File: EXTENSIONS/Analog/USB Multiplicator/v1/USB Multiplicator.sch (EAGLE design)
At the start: 9 parts, among them X1 USB-A

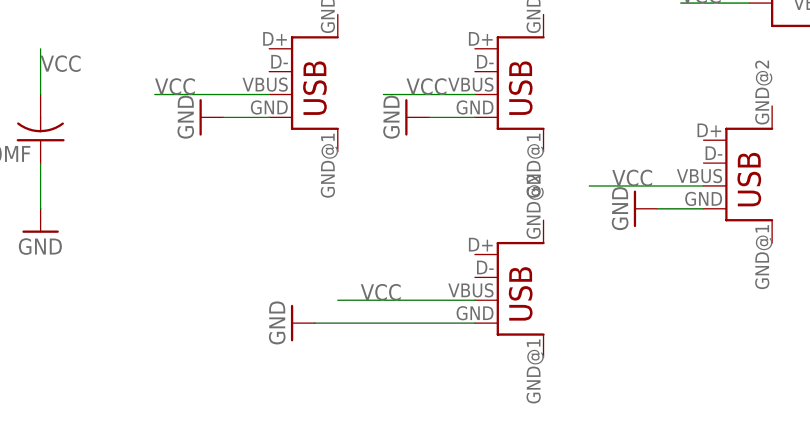
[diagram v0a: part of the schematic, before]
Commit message: Created 4017-7Segment v2
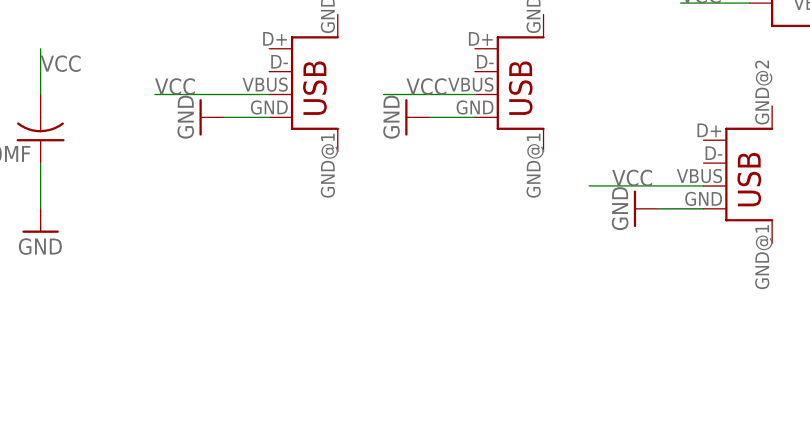
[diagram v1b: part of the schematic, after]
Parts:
- removed USB_OUT_5: USB, STUNTAZ:USB
- renumbered USB_OUT_WITH_DATA_1 to USB_OUT_1
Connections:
- net GND: no longer USB_OUT_5.GND
- net VCC: no longer USB_OUT_5.VBUS
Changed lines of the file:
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@@
 <part name="R_1K" library="adafruit" deviceset="R-US_" device="R1206"/>
 <part name="GND7" library="supply1" deviceset="GND" device=""/>
-<part name="USB_OUT_WITH_DATA_1" library="STUNTAZ" deviceset="USB" device=""/>
+<part name="USB_OUT_1" library="STUNTAZ" deviceset="USB" device=""/>
 <part name="GND2" library="supply1" deviceset="GND" device=""/>
 <part name="USB_OUT_2" library="STUNTAZ" deviceset="USB" device=""/>
@@
 <part name="GND4" library="supply1" deviceset="GND" device=""/>
 <part name="GND5" library="supply1" deviceset="GND" device=""/>
-<part name="USB_OUT_5" library="STUNTAZ" deviceset="USB" device=""/>
-<part name="GND8" library="supply1" deviceset="GND" device=""/>
 </parts>
 <sheets>
@@
 <instance part="R_1K" gate="G$1" x="-12.7" y="81.28" rot="R90"/>
 <instance part="GND7" gate="1" x="-12.7" y="68.58"/>
-<instance part="USB_OUT_WITH_DATA_1" gate="G$1" x="55.88" y="104.14"/>
+<instance part="USB_OUT_1" gate="G$1" x="55.88" y="104.14"/>
 <instance part="GND2" gate="1" x="35.56" y="106.68" rot="R270"/>
 <instance part="USB_OUT_2" gate="G$1" x="66.04" y="78.74"/>
@@
 <instance part="GND4" gate="1" x="78.74" y="81.28" rot="R270"/>
 <instance part="GND5" gate="1" x="104.14" y="71.12" rot="R270"/>
-<instance part="USB_OUT_5" gate="G$1" x="88.9" y="55.88"/>
-<instance part="GND8" gate="1" x="66.04" y="58.42" rot="R270"/>
 </instances>
 <busses>
@@
 </segment>
 <segment>
-<pinref part="USB_OUT_WITH_DATA_1" gate="G$1" pin="GND"/>
+<pinref part="USB_OUT_1" gate="G$1" pin="GND"/>
 <pinref part="GND2" gate="1" pin="GND"/>
 <wire x1="53.34" y1="106.68" x2="38.1" y2="106.68" width="0.1524" layer="91"/>
@@
 <pinref part="USB_OUT_4" gate="G$1" pin="GND"/>
 <wire x1="106.68" y1="71.12" x2="111.76" y2="71.12" width="0.1524" layer="91"/>
-</segment>
-<segment>
-<pinref part="USB_OUT_5" gate="G$1" pin="GND"/>
-<pinref part="GND8" gate="1" pin="GND"/>
-<wire x1="86.36" y1="58.42" x2="68.58" y2="58.42" width="0.1524" layer="91"/>
 </segment>
 </net>
@@
 </segment>
 <segment>
-<pinref part="USB_OUT_WITH_DATA_1" gate="G$1" pin="VBUS"/>
+<pinref part="USB_OUT_1" gate="G$1" pin="VBUS"/>
 <wire x1="53.34" y1="109.22" x2="30.48" y2="109.22" width="0.1524" layer="91"/>
 <label x="35.56" y="109.22" size="1.778" layer="95"/>
@@
 <label x="101.6" y="73.66" size="1.778" layer="95"/>
 </segment>
-<segment>
-<pinref part="USB_OUT_5" gate="G$1" pin="VBUS"/>
-<wire x1="86.36" y1="60.96" x2="71.12" y2="60.96" width="0.1524" layer="91"/>
-<label x="73.66" y="60.96" size="1.778" layer="95"/>
-</segment>
 </net>
 <net name="N$5" class="0">
@@
 </segment>
 <segment>
-<pinref part="USB_OUT_WITH_DATA_1" gate="G$1" pin="D-"/>
+<pinref part="USB_OUT_1" gate="G$1" pin="D-"/>
 <wire x1="53.34" y1="111.76" x2="17.78" y2="111.76" width="0.1524" layer="91"/>
 <label x="20.32" y="111.76" size="1.778" layer="95"/>
@@
 </segment>
 <segment>
-<pinref part="USB_OUT_WITH_DATA_1" gate="G$1" pin="D+"/>
+<pinref part="USB_OUT_1" gate="G$1" pin="D+"/>
 <wire x1="53.34" y1="114.3" x2="25.4" y2="114.3" width="0.1524" layer="91"/>
 <label x="27.94" y="116.84" size="1.778" layer="95"/>
